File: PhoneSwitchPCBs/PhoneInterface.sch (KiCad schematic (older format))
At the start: 52 parts, among them J1 Interface, J2 6P2C, K1 EC2-5NU, K2 EC2-5NU, K3 EC2-5NU, K4 EC2-5NU, K5 EC2-5NU, Q1 PHPT61003PYX, Q2 PHPT61003NYX, Q3 XP231N02013R-G, Q4 XP231N02013R-G, Q5 XP231N02013R-G, Q6 XP231N02013R-G, U1 TCMD1000, U2 NL17SZ14DBVT1G

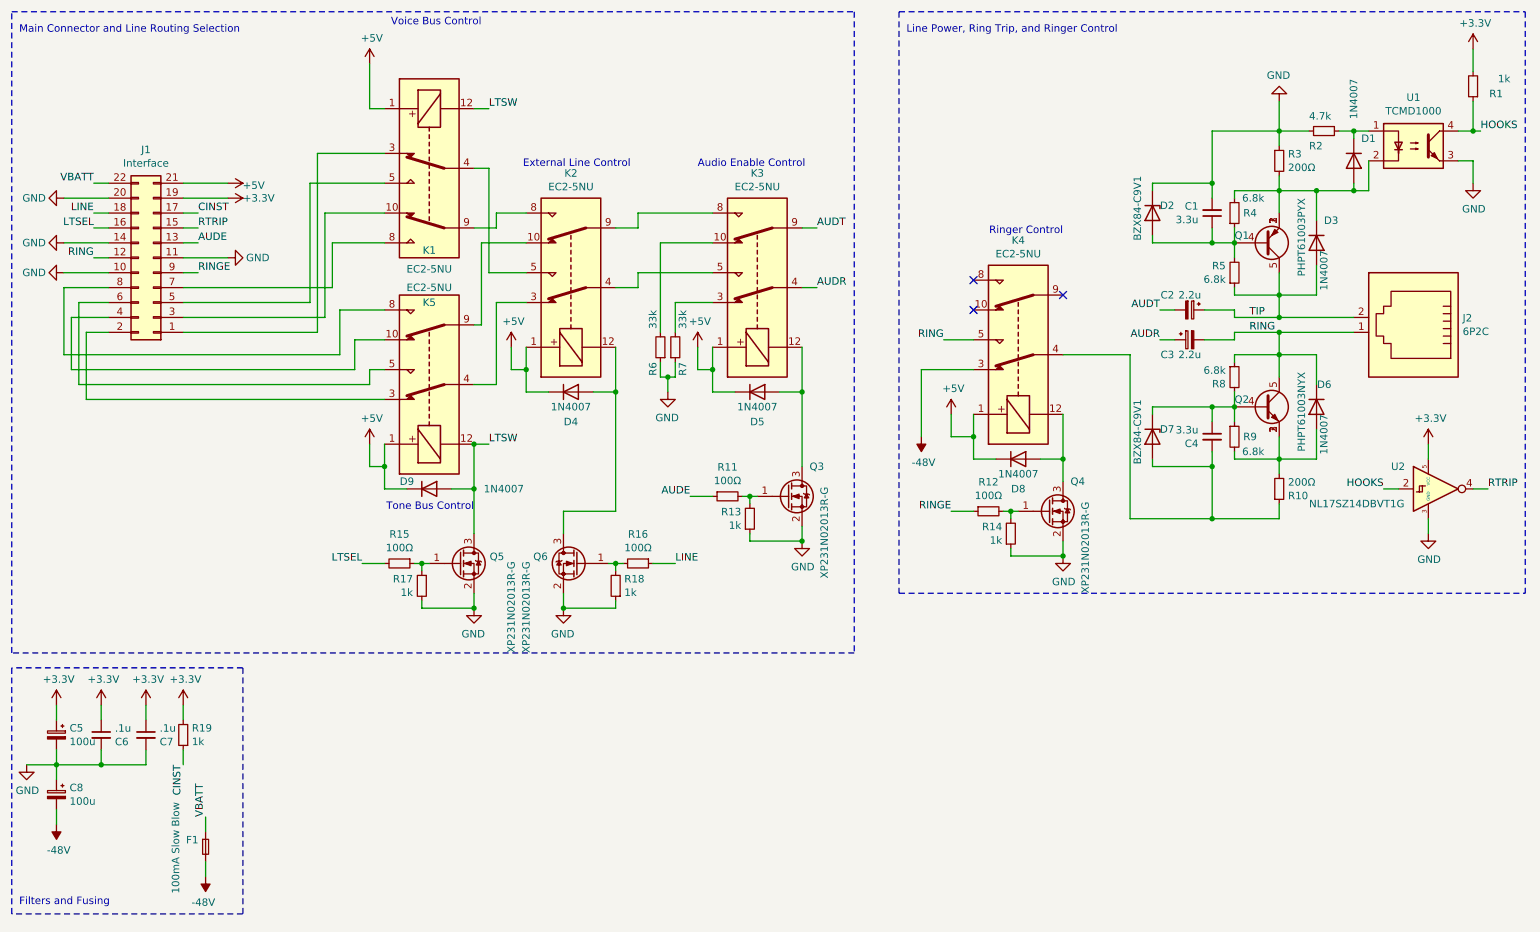
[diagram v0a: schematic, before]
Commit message: Start initial PCB layout, fix some small mistakes in schematic
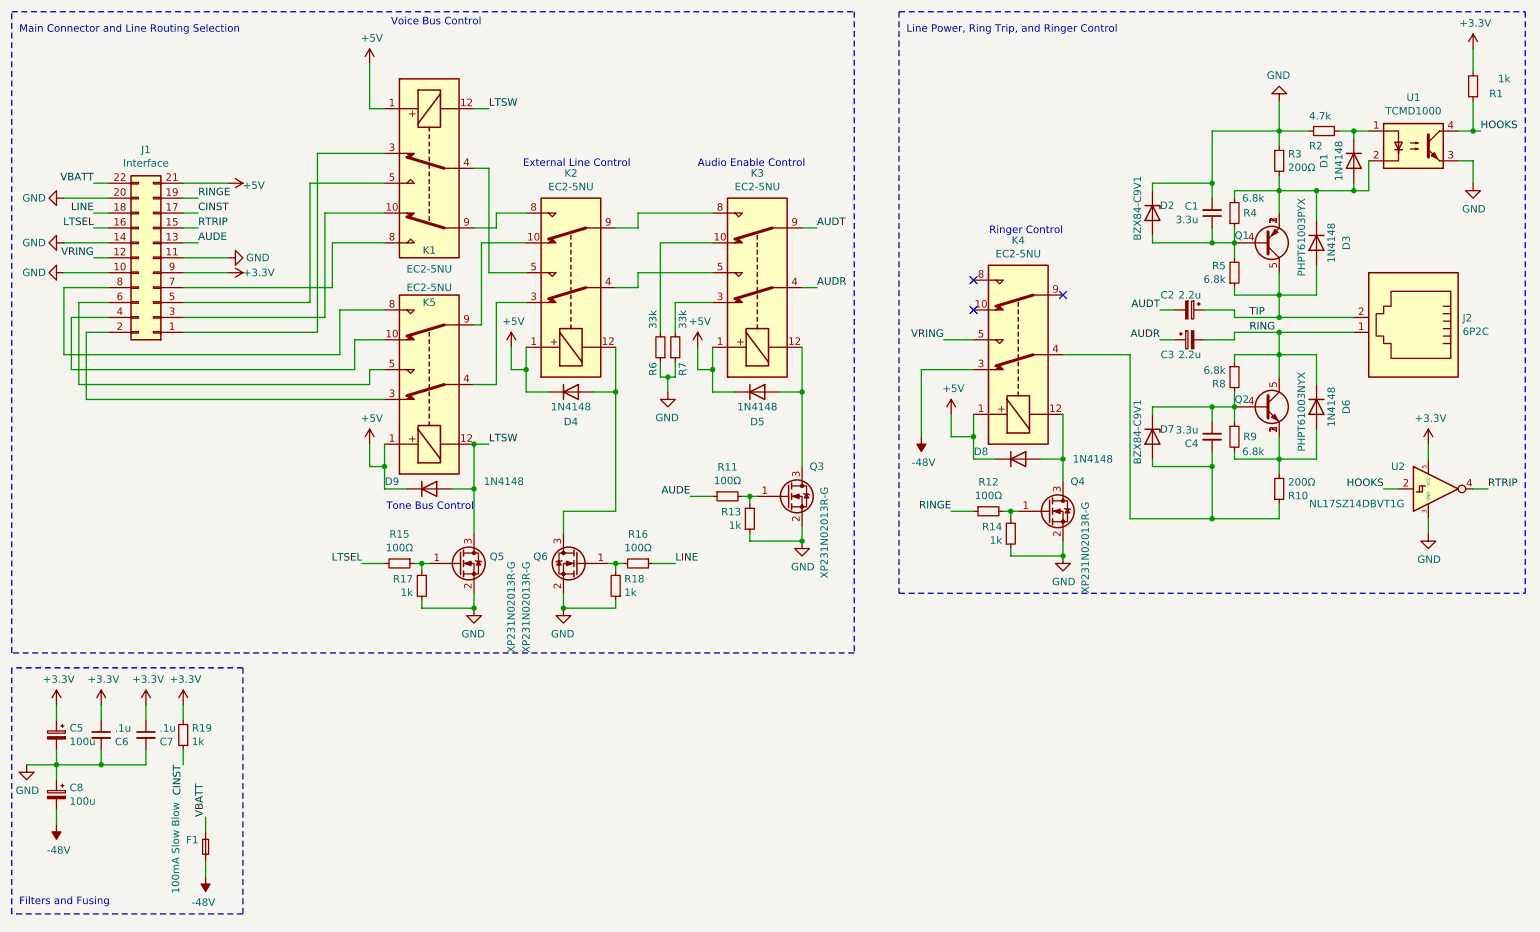
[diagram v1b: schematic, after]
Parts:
- removed D1, D3, D4, D5, D6, D8, D9: 1N4007, Diode_THT:D_DO-41_SOD81_P10.16mm_Horizontal, symbol Diode:1N4007
- added D1, D3, D4, D5, D6, D8, D9: 1N4148, Diode_THT:D_DO-35_SOD27_P7.62mm_Horizontal, symbol Diode:1N4148
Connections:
- net +3V3: now also J1.9 (Pin_9); no longer J1.19 (Pin_19)
- net +5V: now also D4.1 (K), D5.1 (K), D8.1 (K), D9.1 (K)
- net LTSW: now also D9.2 (A)
- net RING: now also D6.1 (K); no longer J1.12 (Pin_12), K4.5
- net RINGE: now also J1.19 (Pin_19); no longer J1.9 (Pin_9)
- net TIP: now also D3.2 (A)
- net at Q1.1 (E), Q1.2 (E), Q1.3 (E)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: now also D1.2 (A), D3.1 (K)
- net at Q2.1 (E), Q2.2 (E), Q2.3 (E)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: now also D6.2 (A)
- net at K4.12, Q4.3 (D): now also D8.2 (A)
- net at R2.1, U1.1: now also D1.1 (K)
- net at K3.12, Q3.3 (D): now also D5.2 (A)
- net at K2.12, Q6.3 (D): now also D4.2 (A)
- new net VRING: J1.12 (Pin_12), K4.5
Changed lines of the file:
@@
 	9250 1450 9250 1250
 Connection ~ 9250 1450
-$Comp
-L Diode:1N4007 D3
-U 1 1 60F4828E
-P 9500 2200
-F 0 "D3" V 9350 2250 50  0000 L CNN
-F 1 "1N4007" H 9550 2250 50  0000 L CNN
-F 2 "Diode_THT:D_DO-41_SOD81_P10.16mm_Horizontal" H 9500 2025 50  0001 C CNN
-F 3 "http://www.vishay.com/docs/88503/1n4001.pdf" H 9500 2200 50  0001 C CNN
-	1    9500 2200
-	0    1    1    0
-$EndComp
 Wire Wire Line
 	9500 2050 9500 1850
@@
 Wire Wire Line
 	9250 4050 9250 3950
-$Comp
-L Diode:1N4007 D6
-U 1 1 60F4F891
-P 9500 3300
-F 0 "D6" V 9350 3200 50  0000 L CNN
-F 1 "1N4007" H 9550 3250 50  0000 L CNN
-F 2 "Diode_THT:D_DO-41_SOD81_P10.16mm_Horizontal" H 9500 3125 50  0001 C CNN
-F 3 "http://www.vishay.com/docs/88503/1n4001.pdf" H 9500 3300 50  0001 C CNN
-	1    9500 3300
-	0    -1   1    0
-$EndComp
 Wire Wire Line
 	9500 3450 9500 3650
@@
 	9650 1450 9750 1450
 Connection ~ 9500 1850
-$Comp
-L Diode:1N4007 D1
-U 1 1 60F9656B
-P 9750 1650
-F 0 "D1" V 9600 1700 50  0000 L CNN
-F 1 "1N4007" H 9200 1650 50  0000 L CNN
-F 2 "Diode_THT:D_DO-41_SOD81_P10.16mm_Horizontal" H 9750 1475 50  0001 C CNN
-F 3 "http://www.vishay.com/docs/88503/1n4001.pdf" H 9750 1650 50  0001 C CNN
-	1    9750 1650
-	0    1    1    0
-$EndComp
 Wire Wire Line
 	9850 1850 9850 1650
@@
 	0    -1   -1   0
 $EndComp
-$Comp
-L Diode:1N4007 D8
-U 1 1 60FF02D6
-P 7500 3650
-F 0 "D8" H 7500 3450 50  0000 C CNN
-F 1 "1N4007" H 7500 3550 50  0000 C CNN
-F 2 "Diode_THT:D_DO-41_SOD81_P10.16mm_Horizontal" H 7500 3475 50  0001 C CNN
-F 3 "http://www.vishay.com/docs/88503/1n4001.pdf" H 7500 3650 50  0001 C CNN
-	1    7500 3650
-	1    0    0    -1
-$EndComp
-$Comp
-L Diode:1N4007 D5
-U 1 1 60FF183F
-P 5750 3200
-F 0 "D5" H 5750 3000 50  0000 C CNN
-F 1 "1N4007" H 5750 3100 50  0000 C CNN
-F 2 "Diode_THT:D_DO-41_SOD81_P10.16mm_Horizontal" H 5750 3025 50  0001 C CNN
-F 3 "http://www.vishay.com/docs/88503/1n4001.pdf" H 5750 3200 50  0001 C CNN
-	1    5750 3200
-	1    0    0    -1
-$EndComp
-$Comp
-L Diode:1N4007 D4
-U 1 1 60FF2753
-P 4500 3200
-F 0 "D4" H 4500 3000 50  0000 C CNN
-F 1 "1N4007" H 4500 3100 50  0000 C CNN
-F 2 "Diode_THT:D_DO-41_SOD81_P10.16mm_Horizontal" H 4500 3025 50  0001 C CNN
-F 3 "http://www.vishay.com/docs/88503/1n4001.pdf" H 4500 3200 50  0001 C CNN
-	1    4500 3200
-	1    0    0    -1
-$EndComp
 Wire Wire Line
 	7650 3650 7800 3650
@@
 Wire Wire Line
 	4200 3200 4350 3200
-$Comp
-L Diode:1N4007 D9
-U 1 1 61025FFB
-P 3550 3850
-F 0 "D9" H 3400 3900 50  0000 C CNN
-F 1 "1N4007" H 4050 3850 50  0000 C CNN
-F 2 "Diode_THT:D_DO-41_SOD81_P10.16mm_Horizontal" H 3550 3675 50  0001 C CNN
-F 3 "http://www.vishay.com/docs/88503/1n4001.pdf" H 3550 3850 50  0001 C CNN
-	1    3550 3850
-	1    0    0    -1
-$EndComp
 Wire Wire Line
 	3700 3850 3850 3850
@@
 Line Power, Ring Trip, and Ringer Control
 Text Label 1300 2300 2    50   ~ 0
-RING
+VRING
 Text Label 6150 2100 0    50   ~ 0
 AUDT
@@
 Wire Wire Line
 	5050 4350 5200 4350
-Text Label 2000 2400 0    50   ~ 0
+Text Label 2000 1900 0    50   ~ 0
 RINGE
 Text Label 2000 2200 0    50   ~ 0
@@
 	1300 1800 1400 1800
 $Comp
-L power:+3.3V #PWR0120
-U 1 1 6125ADE8
-P 2200 1900
-F 0 "#PWR0120" H 2200 1750 50  0001 C CNN
-F 1 "+3.3V" V 2200 2000 50  0000 L CNN
-F 2 "" H 2200 1900 50  0001 C CNN
-F 3 "" H 2200 1900 50  0001 C CNN
-	1    2200 1900
-	0    1    1    0
-$EndComp
-$Comp
 L power:GND #PWR0121
 U 1 1 6126D62F
@@
 $EndComp
 Text Label 7000 2850 2    50   ~ 0
-RING
+VRING
 Wire Wire Line
 	7200 2850 7000 2850
@@
 $EndComp
 Wire Wire Line
-	1900 2400 2000 2400
-Wire Wire Line
-	1900 1900 2200 1900
-Wire Wire Line
 	1100 1900 1400 1900
 Wire Wire Line
@@
 	0    1    1    0
 $EndComp
+$Comp
+L Diode:1N4148 D5
+U 1 1 6102E0C1
+P 5750 3200
+F 0 "D5" H 5750 3000 50  0000 C CNN
+F 1 "1N4148" H 5750 3100 50  0000 C CNN
+F 2 "Diode_THT:D_DO-35_SOD27_P7.62mm_Horizontal" H 5750 3025 50  0001 C CNN
+F 3 "https://assets.nexperia.com/documents/data-sheet/1N4148_1N4448.pdf" H 5750 3200 50  0001 C CNN
+	1    5750 3200
+	1    0    0    -1
+$EndComp
+$Comp
+L Diode:1N4148 D4
+U 1 1 6102EA3B
+P 4500 3200
+F 0 "D4" H 4500 3000 50  0000 C CNN
+F 1 "1N4148" H 4500 3100 50  0000 C CNN
+F 2 "Diode_THT:D_DO-35_SOD27_P7.62mm_Horizontal" H 4500 3025 50  0001 C CNN
+F 3 "https://assets.nexperia.com/documents/data-sheet/1N4148_1N4448.pdf" H 4500 3200 50  0001 C CNN
+	1    4500 3200
+	1    0    0    -1
+$EndComp
+$Comp
+L Diode:1N4148 D9
+U 1 1 6102F2BB
+P 3550 3850
+F 0 "D9" H 3300 3900 50  0000 C CNN
+F 1 "1N4148" H 4050 3900 50  0000 C CNN
+F 2 "Diode_THT:D_DO-35_SOD27_P7.62mm_Horizontal" H 3550 3675 50  0001 C CNN
+F 3 "https://assets.nexperia.com/documents/data-sheet/1N4148_1N4448.pdf" H 3550 3850 50  0001 C CNN
+	1    3550 3850
+	1    0    0    -1
+$EndComp
+$Comp
+L Diode:1N4148 D8
+U 1 1 6102FC8A
+P 7500 3650
+F 0 "D8" H 7250 3700 50  0000 C CNN
+F 1 "1N4148" H 8000 3650 50  0000 C CNN
+F 2 "Diode_THT:D_DO-35_SOD27_P7.62mm_Horizontal" H 7500 3475 50  0001 C CNN
+F 3 "https://assets.nexperia.com/documents/data-sheet/1N4148_1N4448.pdf" H 7500 3650 50  0001 C CNN
+	1    7500 3650
+	1    0    0    -1
+$EndComp
+$Comp
+L Diode:1N4148 D1
+U 1 1 61031863
+P 9750 1650
+F 0 "D1" H 9750 1450 50  0000 C CNN
+F 1 "1N4148" H 9750 1550 50  0000 C CNN
+F 2 "Diode_THT:D_DO-35_SOD27_P7.62mm_Horizontal" H 9750 1475 50  0001 C CNN
+F 3 "https://assets.nexperia.com/documents/data-sheet/1N4148_1N4448.pdf" H 9750 1650 50  0001 C CNN
+	1    9750 1650
+	0    1    1    0
+$EndComp
+$Comp
+L Diode:1N4148 D3
+U 1 1 6107602F
+P 9500 2200
+F 0 "D3" H 9500 2000 50  0000 C CNN
+F 1 "1N4148" H 9500 2100 50  0000 C CNN
+F 2 "Diode_THT:D_DO-35_SOD27_P7.62mm_Horizontal" H 9500 2025 50  0001 C CNN
+F 3 "https://assets.nexperia.com/documents/data-sheet/1N4148_1N4448.pdf" H 9500 2200 50  0001 C CNN
+	1    9500 2200
+	0    -1   1    0
+$EndComp
+$Comp
+L Diode:1N4148 D6
+U 1 1 61076B49
+P 9500 3300
+F 0 "D6" H 9500 3100 50  0000 C CNN
+F 1 "1N4148" H 9500 3200 50  0000 C CNN
+F 2 "Diode_THT:D_DO-35_SOD27_P7.62mm_Horizontal" H 9500 3125 50  0001 C CNN
+F 3 "https://assets.nexperia.com/documents/data-sheet/1N4148_1N4448.pdf" H 9500 3300 50  0001 C CNN
+	1    9500 3300
+	0    -1   1    0
+$EndComp
+$Comp
+L power:+3.3V #PWR0120
+U 1 1 6125ADE8
+P 2200 2400
+F 0 "#PWR0120" H 2200 2250 50  0001 C CNN
+F 1 "+3.3V" V 2200 2500 50  0000 L CNN
+F 2 "" H 2200 2400 50  0001 C CNN
+F 3 "" H 2200 2400 50  0001 C CNN
+	1    2200 2400
+	0    1    1    0
+$EndComp
+Wire Wire Line
+	2000 1900 1900 1900
+Wire Wire Line
+	1900 2400 2200 2400
 $EndSCHEMATC

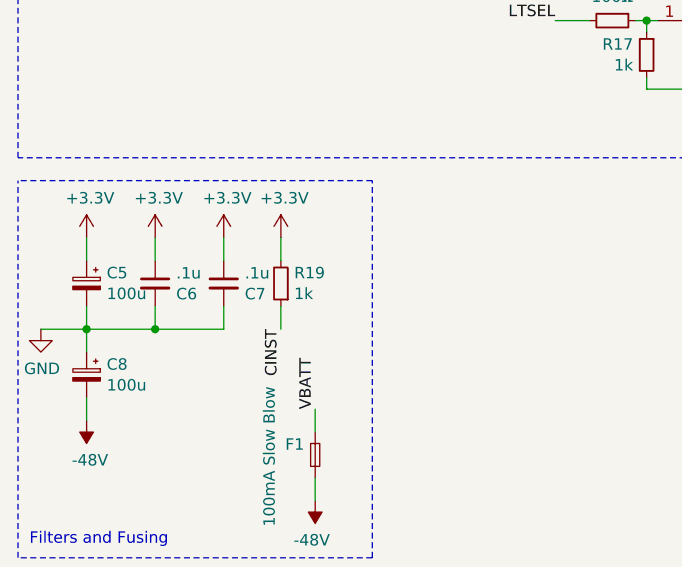
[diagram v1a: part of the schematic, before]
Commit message: tweaked detect resistor to pulldown, finished routing all tracks!
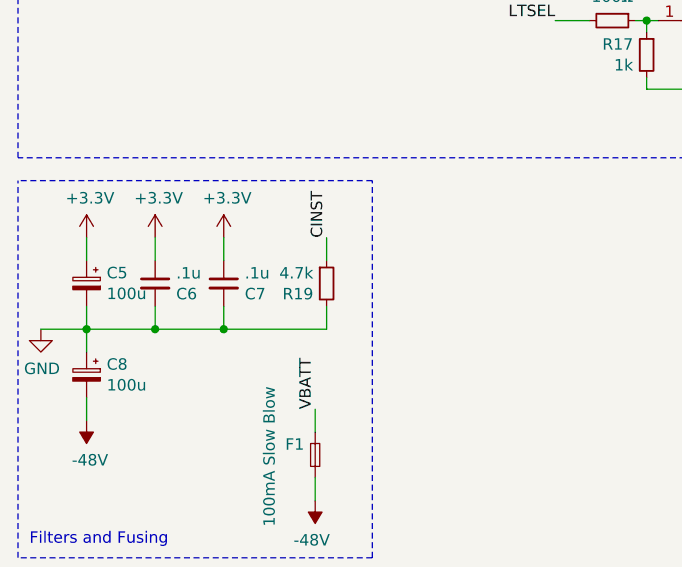
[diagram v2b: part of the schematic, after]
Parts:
- R19: value 1k -> 4.7k
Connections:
- net +3V3: no longer R19.2
- net GND: now also R19.2
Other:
- moved on the sheet: R19
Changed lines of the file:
@@
 L Device:R_Small R19
 U 1 1 60FEA6CF
-P 1900 5500
-F 0 "R19" H 1842 5454 50  0000 R CNN
-F 1 "1k" H 1842 5545 50  0000 R CNN
-F 2 "Resistor_SMD:R_0805_2012Metric_Pad1.20x1.40mm_HandSolder" H 1900 5500 50  0001 C CNN
-F 3 "~" H 1900 5500 50  0001 C CNN
-	1    1900 5500
-	-1   0    0    1
-$EndComp
-$Comp
-L power:+3.3V #PWR0127
-U 1 1 61012BD6
-P 1900 5300
-F 0 "#PWR0127" H 1900 5150 50  0001 C CNN
-F 1 "+3.3V" H 1915 5473 50  0000 C CNN
-F 2 "" H 1900 5300 50  0001 C CNN
-F 3 "" H 1900 5300 50  0001 C CNN
-	1    1900 5300
-	1    0    0    -1
-$EndComp
-Wire Wire Line
-	1900 5400 1900 5300
-Text Label 1900 5700 3    50   ~ 0
+P 2100 5500
+F 0 "R19" H 2042 5454 50  0000 R CNN
+F 1 "4.7k" H 2042 5545 50  0000 R CNN
+F 2 "Resistor_SMD:R_0805_2012Metric_Pad1.20x1.40mm_HandSolder" H 2100 5500 50  0001 C CNN
+F 3 "~" H 2100 5500 50  0001 C CNN
+	1    2100 5500
+	1    0    0    -1
+$EndComp
+Wire Wire Line
+	2100 5600 2100 5700
+Text Label 2100 5300 1    50   ~ 0
 CINST
 Wire Wire Line
-	1900 5700 1900 5600
+	2100 5300 2100 5400
 Wire Wire Line
 	1100 2400 1400 2400
@@
 Wire Wire Line
 	1900 2400 2200 2400
+Wire Wire Line
+	2100 5700 1650 5700
+Connection ~ 1650 5700
 $EndSCHEMATC

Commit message: Update schematic PDF
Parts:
- added H1: MNT1, MountingHole:MountingHole_2.7mm_M2.5_Pad, symbol Mechanical:MountingHole_Pad
- added H2: MNT2, MountingHole:MountingHole_2.7mm_M2.5_Pad, symbol Mechanical:MountingHole_Pad
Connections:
- net GND: now also H1.1, H2.1
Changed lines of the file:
@@
 	2100 5700 1650 5700
 Connection ~ 1650 5700
+$Comp
+L Mechanical:MountingHole_Pad H1
+U 1 1 61033A10
+P 1350 6150
+F 0 "H1" H 1300 6100 50  0000 R CNN
+F 1 "MNT1" H 1450 6350 50  0000 R CNN
+F 2 "MountingHole:MountingHole_2.7mm_M2.5_Pad" H 1350 6150 50  0001 C CNN
+F 3 "~" H 1350 6150 50  0001 C CNN
+	1    1350 6150
+	-1   0    0    1
+$EndComp
+$Comp
+L Mechanical:MountingHole_Pad H2
+U 1 1 61034116
+P 1650 6150
+F 0 "H2" H 1600 6100 50  0000 R CNN
+F 1 "MNT2" H 1750 6350 50  0000 R CNN
+F 2 "MountingHole:MountingHole_2.7mm_M2.5_Pad" H 1650 6150 50  0001 C CNN
+F 3 "~" H 1650 6150 50  0001 C CNN
+	1    1650 6150
+	-1   0    0    1
+$EndComp
+Wire Wire Line
+	1650 6050 1650 5700
+Wire Wire Line
+	1350 5700 1350 6050
 $EndSCHEMATC

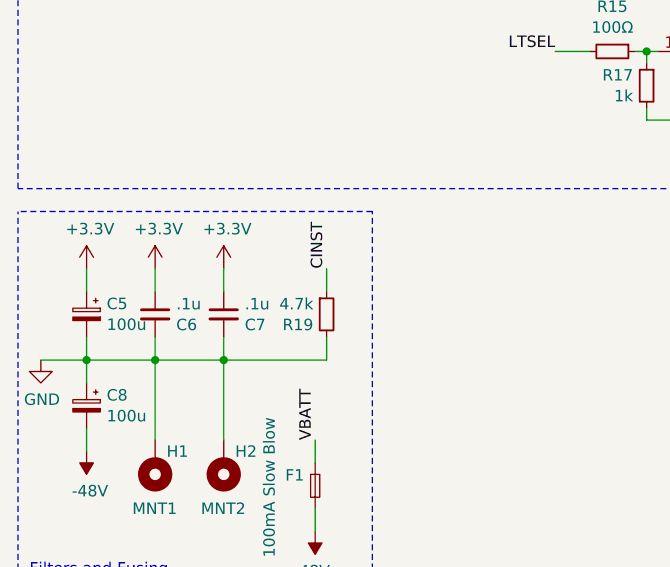
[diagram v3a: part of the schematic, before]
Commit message: Remove extra cap from schematic, finish up PCB design
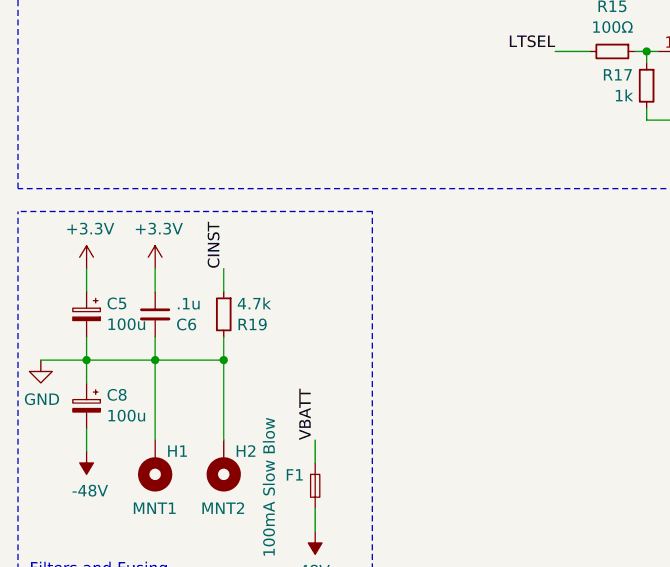
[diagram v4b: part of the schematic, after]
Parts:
- removed C7: .1u, Capacitor_SMD:C_0603_1608Metric_Pad1.08x0.95mm_HandSolder, symbol Device:C_Small
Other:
- moved on the sheet: R19
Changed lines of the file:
@@
 Wire Wire Line
 	1350 5700 1050 5700
-$Comp
-L Device:C_Small C7
-U 1 1 6115AB08
-P 1650 5500
-F 0 "C7" H 1558 5454 50  0000 R CNN
-F 1 ".1u" H 1558 5545 50  0000 R CNN
-F 2 "Capacitor_SMD:C_0603_1608Metric_Pad1.08x0.95mm_HandSolder" H 1650 5500 50  0001 C CNN
-F 3 "~" H 1650 5500 50  0001 C CNN
-	1    1650 5500
-	-1   0    0    -1
-$EndComp
-Wire Wire Line
-	1650 5300 1650 5400
 Wire Wire Line
 	1650 5700 1350 5700
-Wire Wire Line
-	1650 5600 1650 5700
 Connection ~ 1350 5700
 Text Label 1300 1800 2    50   ~ 0
@@
 $EndComp
 $Comp
-L power:+3.3V #PWR0124
-U 1 1 61280978
-P 1650 5300
-F 0 "#PWR0124" H 1650 5150 50  0001 C CNN
-F 1 "+3.3V" H 1665 5473 50  0000 C CNN
-F 2 "" H 1650 5300 50  0001 C CNN
-F 3 "" H 1650 5300 50  0001 C CNN
-	1    1650 5300
-	1    0    0    -1
-$EndComp
-$Comp
 L power:+3.3V #PWR0125
 U 1 1 61280F81
@@
 L Device:R_Small R19
 U 1 1 60FEA6CF
-P 2100 5500
-F 0 "R19" H 2042 5454 50  0000 R CNN
-F 1 "4.7k" H 2042 5545 50  0000 R CNN
-F 2 "Resistor_SMD:R_0805_2012Metric_Pad1.20x1.40mm_HandSolder" H 2100 5500 50  0001 C CNN
-F 3 "~" H 2100 5500 50  0001 C CNN
-	1    2100 5500
-	1    0    0    -1
-$EndComp
-Wire Wire Line
-	2100 5600 2100 5700
-Text Label 2100 5300 1    50   ~ 0
+P 1650 5500
+F 0 "R19" H 1592 5454 50  0000 R CNN
+F 1 "4.7k" H 1592 5545 50  0000 R CNN
+F 2 "Resistor_SMD:R_0805_2012Metric_Pad1.20x1.40mm_HandSolder" H 1650 5500 50  0001 C CNN
+F 3 "~" H 1650 5500 50  0001 C CNN
+	1    1650 5500
+	-1   0    0    -1
+$EndComp
+Wire Wire Line
+	1650 5600 1650 5700
+Text Label 1650 5300 1    50   ~ 0
 CINST
 Wire Wire Line
-	2100 5300 2100 5400
+	1650 5300 1650 5400
 Wire Wire Line
 	1100 2400 1400 2400
@@
 Wire Wire Line
 	1900 2400 2200 2400
-Wire Wire Line
-	2100 5700 1650 5700
 Connection ~ 1650 5700
 $Comp

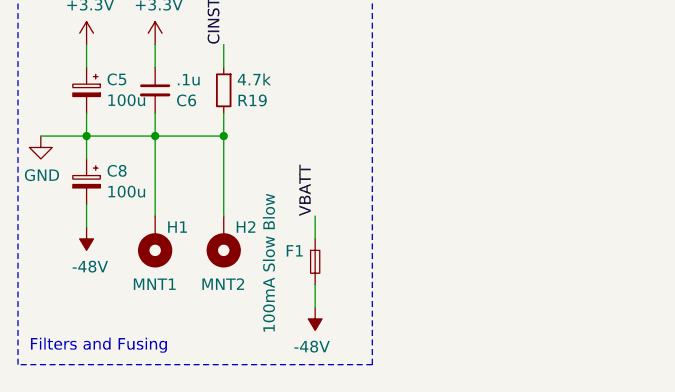
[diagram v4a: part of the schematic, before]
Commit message: Minor tweaks before PCB attempt 2
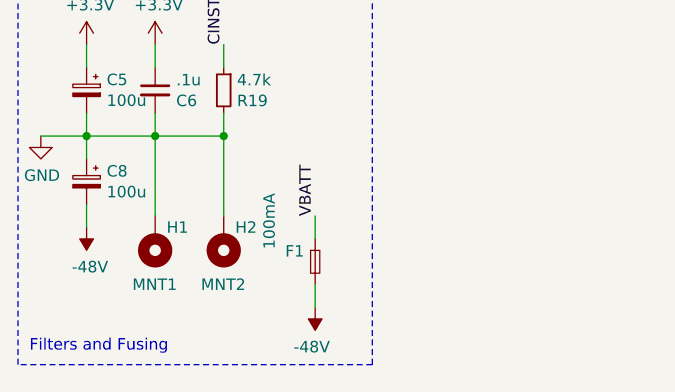
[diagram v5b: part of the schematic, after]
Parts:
- F1: value 100mA Slow Blow -> 100mA
- J2: footprint PhoneInterfaceParts:RJE0112001 -> Imported_Parts:RJE0112001
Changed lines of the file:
@@
 F 0 "J2" H 9820 2896 50  0000 R CNN
 F 1 "6P2C" H 9820 2805 50  0000 R CNN
-F 2 "PhoneInterfaceParts:RJE0112001" V 10150 2825 50  0001 C CNN
+F 2 "Imported_Parts:RJE0112001" V 10150 2825 50  0001 C CNN
 F 3 "~" V 10150 2825 50  0001 C CNN
 	1    10150 2800
@@
 P 2050 6250
 F 0 "F1" V 2004 6298 50  0000 L CNN
-F 1 "100mA Slow Blow" H 1750 6450 50  0000 L CNN
+F 1 "100mA" H 1750 6450 50  0000 L CNN
 F 2 "Imported_Parts:00346605" H 2050 6250 50  0001 C CNN
 F 3 "~" H 2050 6250 50  0001 C CNN
